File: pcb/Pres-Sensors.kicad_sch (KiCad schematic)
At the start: 19 parts, among them J3 SEN0609, J4 LD2410, J6 LD2450, U1 TPS22917DBV, U17 EKMC1603111, U2 TPS22917DBV

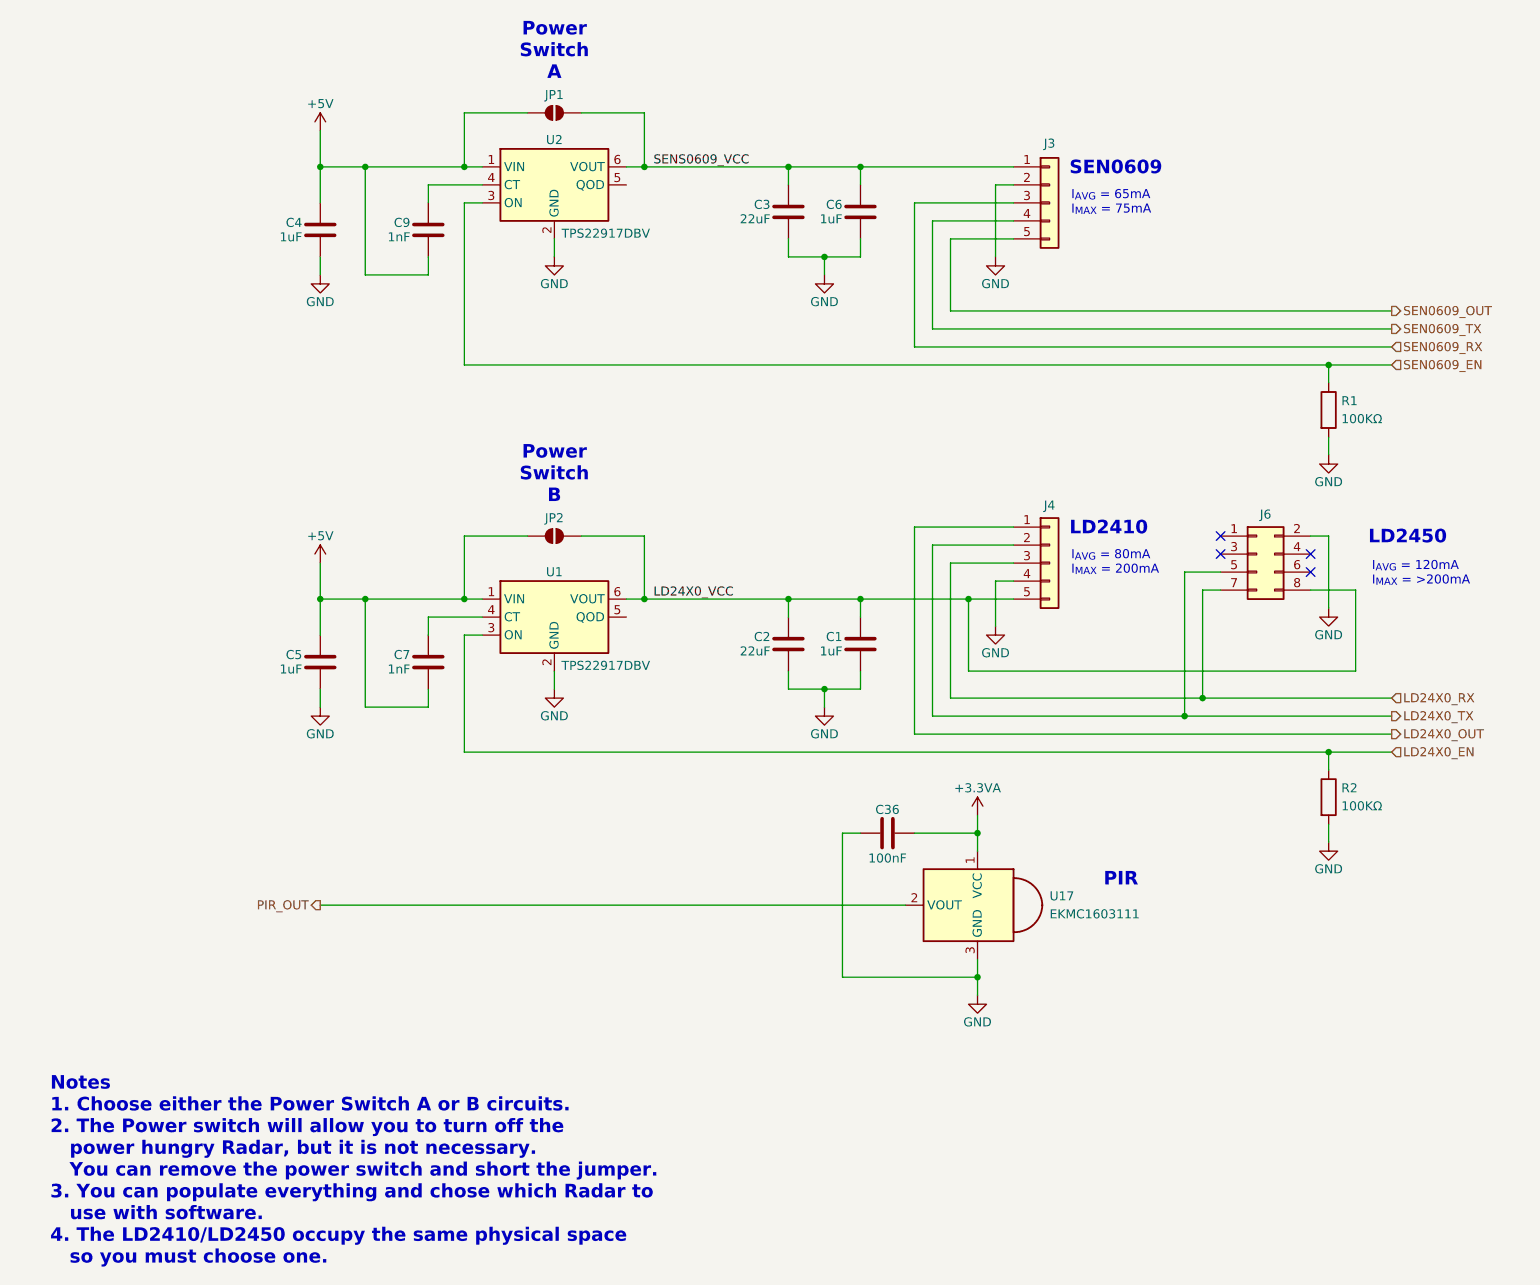
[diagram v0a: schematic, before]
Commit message: Rev A Updates
Support LD2410S and LD2420 Radars in same connector as C4001. Now using 3.3V instead of 5V.
Removed Power control for Radars.
Added DS18S20 to measure CO sensor temperature directly.
Reworked SHT4X layout to reduce thermal transfer.
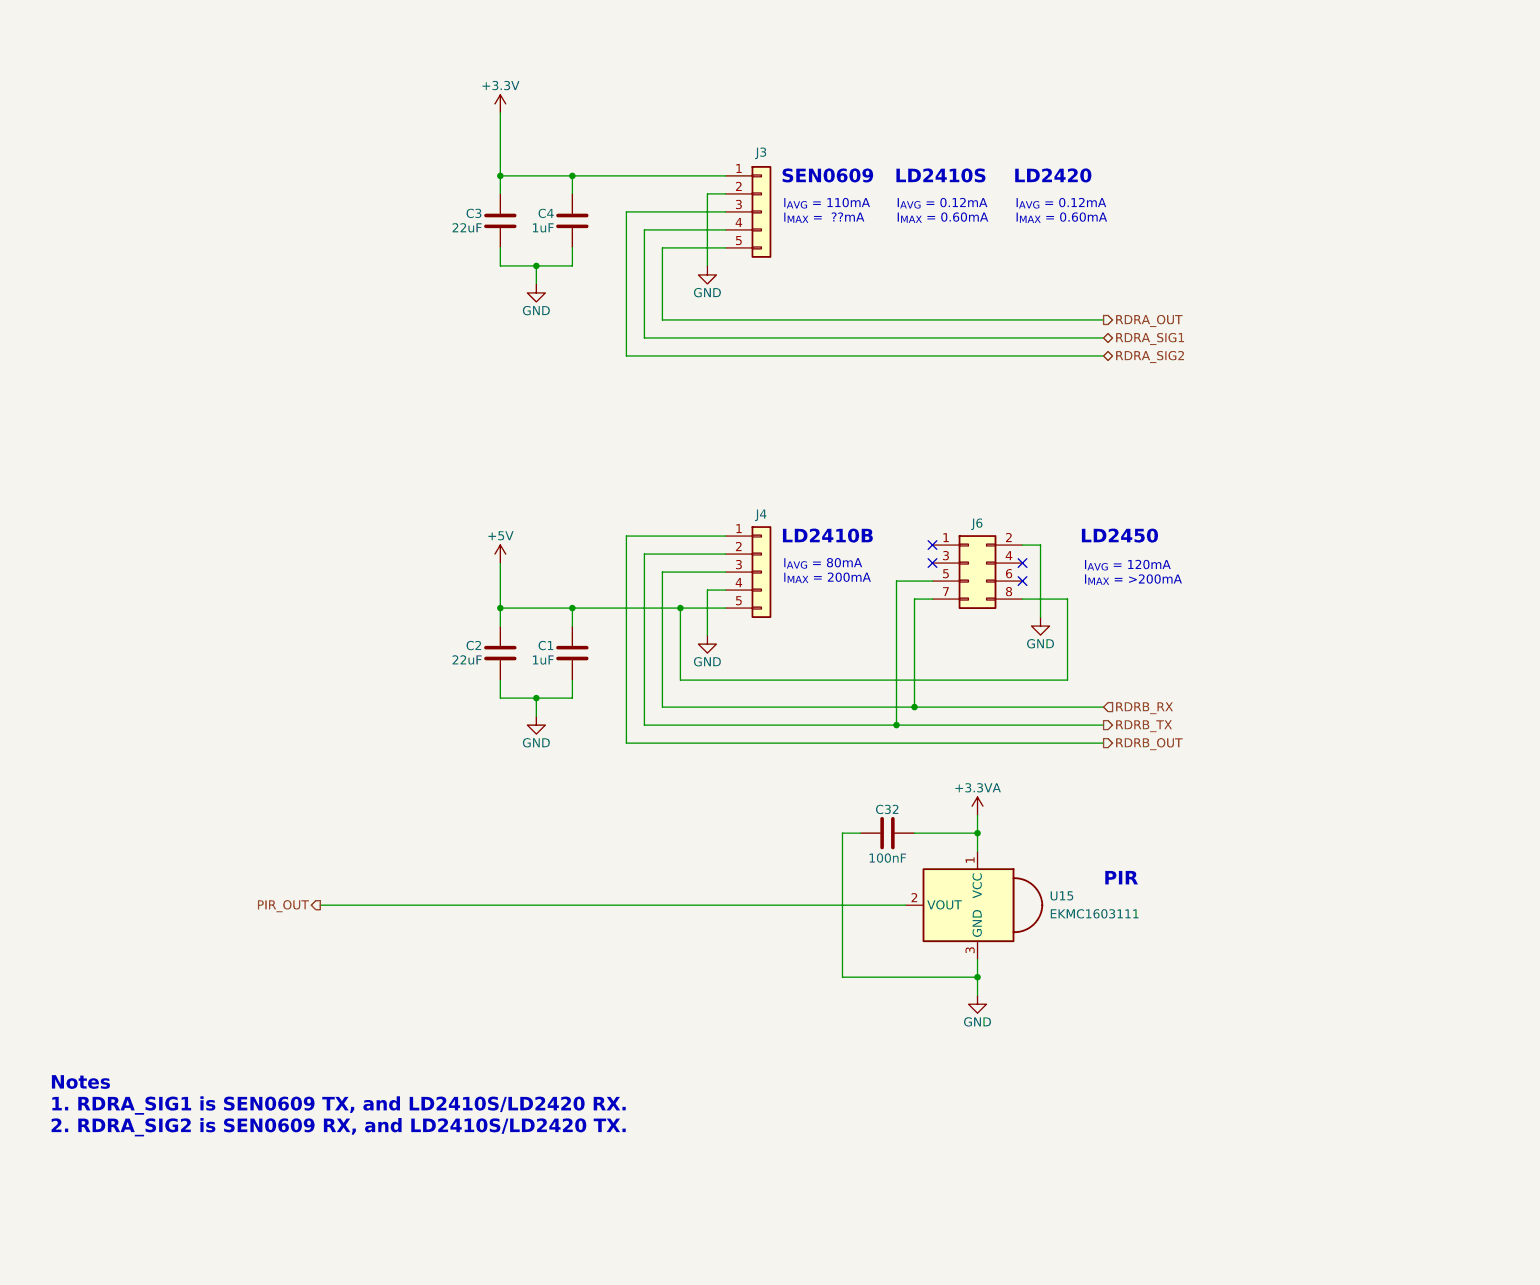
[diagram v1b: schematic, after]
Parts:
- removed C4, C5: 1uF, Capacitor_SMD:C_0402_1005Metric, symbol Device:C
- removed C7, C9: 1nF, Capacitor_SMD:C_0402_1005Metric, symbol Device:C
- removed JP1, JP2: ~, Jumper:SolderJumper-2_P1.3mm_Open_RoundedPad1.0x1.5mm, symbol Jumper:SolderJumper_2_Open
- removed R1, R2: 100KΩ, Resistor_SMD:R_0402_1005Metric, symbol Device:R
- removed U1, U2: TPS22917DBV, Package_TO_SOT_SMD:SOT-23-6, symbol Power_Management:TPS22917DBV
- renumbered C36 to C32, C6 to C4, U17 to U15
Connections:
- net LD24X0_VCC is gone; now on net +5V: C1.1, C2.1, J4.5 (Pin_5), J6.8 (Pin_8)
- net LD24X0_OUT renamed RDRB_OUT
- net LD24X0_RX renamed RDRB_RX
- net LD24X0_TX renamed RDRB_TX
- net SEN0609_OUT renamed RDRA_OUT
- net SEN0609_RX renamed RDRA_SIG2
- net SEN0609_TX renamed RDRA_SIG1
- net SENS0609_VCC renamed +3.3V
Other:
- note added: "I_{AVG} = 0.12mA I_{MAX} = 0.60mA"
- note added: "I_{AVG} = 110mA I_{MAX} = ??mA"
- note added: "LD2410B"
- note added: "LD2410S"
- note added: "LD2420"
- note added: "Notes 1. RDRA_SIG1 is SEN0609 TX, and LD2410S/LD2420 RX. 2. RDRA_SIG2 is SEN0609 RX, and LD2410S/LD2420 TX."
- note removed: "I_{AVG} = 65mA I_{MAX} = 75mA"
- note removed: "LD2410"
- note removed: "Notes 1. Choose either the Power Switch A or B circuits. 2. The Power switch will allow you to turn off the power hungry Radar, but it is not necessary. You can remove the power switch and short the jumper. 3. You can populate everything and chose which Radar to use with software. 4. The LD2410/LD2450 occupy the same physical space so you must choose one."
- note removed: "Power Switch A"
- note removed: "Power Switch B"
- moved on the sheet: C1, C2, C3, C4, J3, J4, J6

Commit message: Rev B Updates finish adding power monitors for 3.3V and 3.3VA
Removed speaker gain jumper
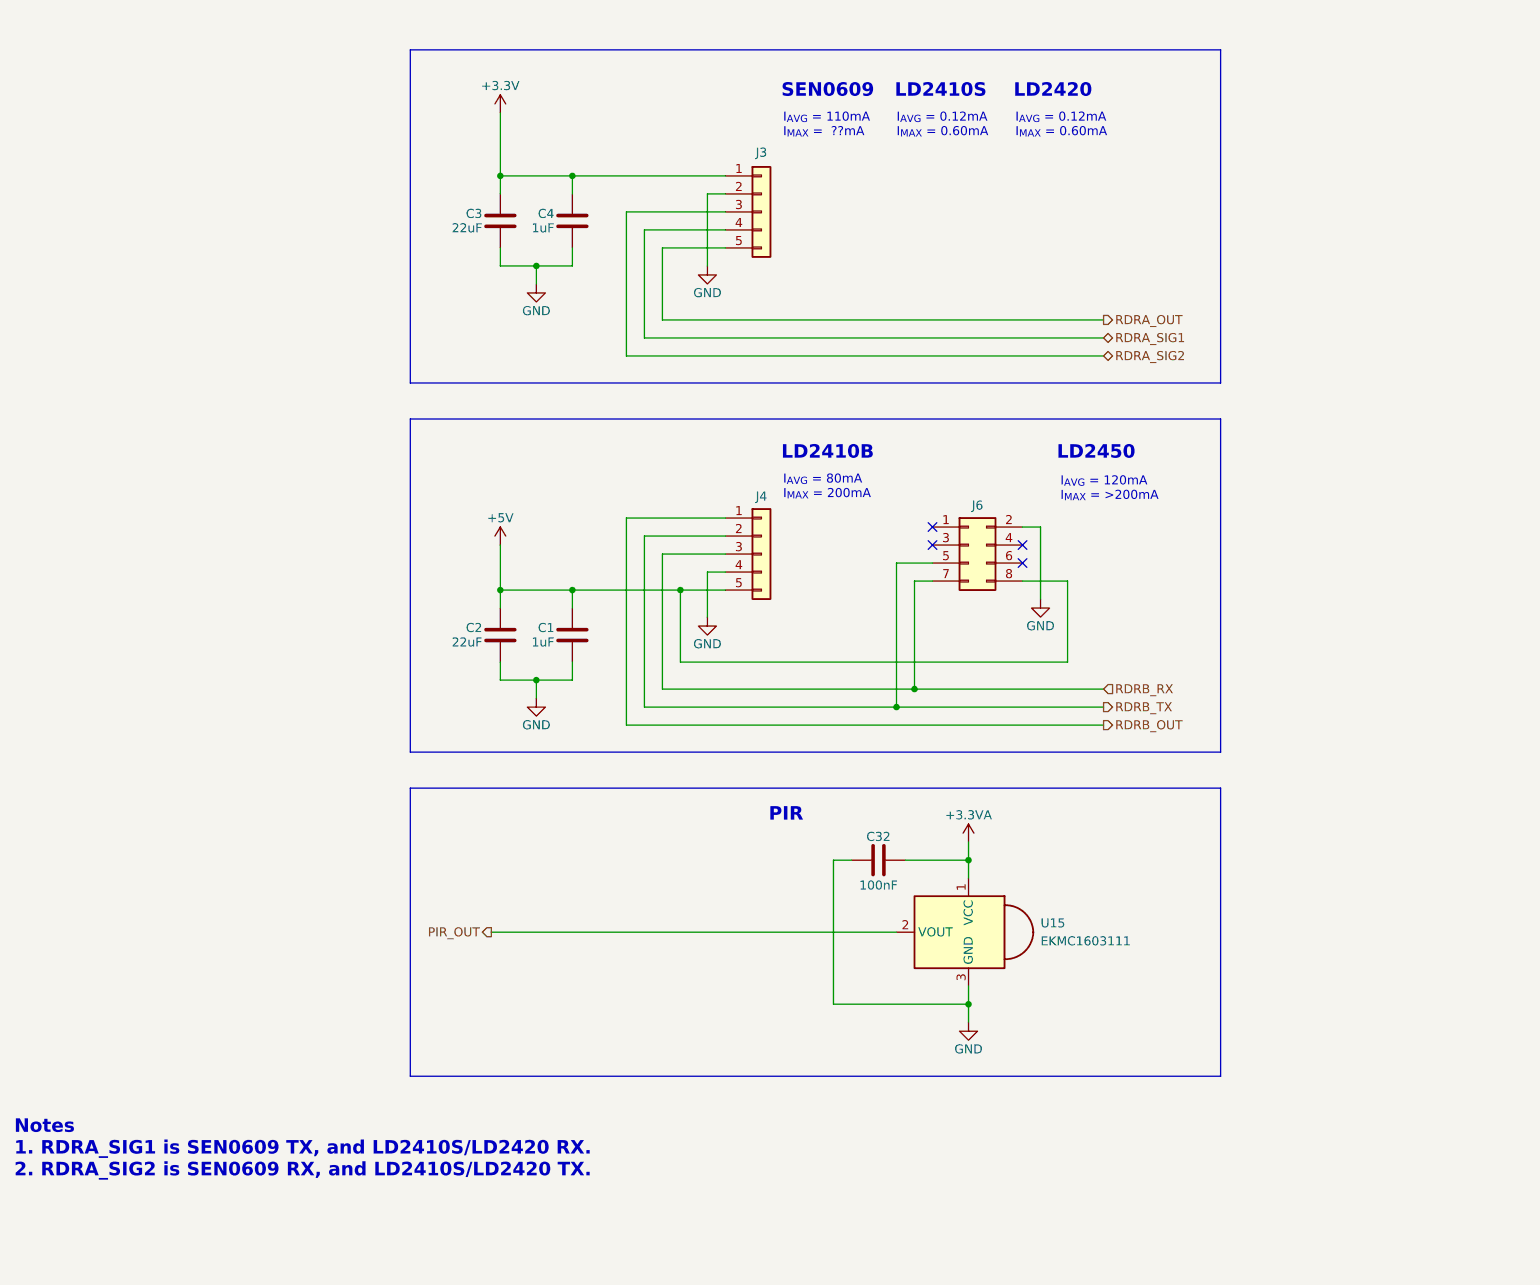
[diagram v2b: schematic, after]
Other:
- title: ESPHome Parking Assistant -> ESPHome Indoor Multi-Sensor
- moved on the sheet: C1, C2, C32, J4, J6, U15
